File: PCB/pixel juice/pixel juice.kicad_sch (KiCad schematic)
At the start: 39 parts, among them J1 n8 Bus Connector, J2 Conn_01x03_Male, J3 PJRAN3X1U03X, U1 TMS9128, U2 TMS4416, U3 TMS4416, U4 74LS32, U5 LM1881, U6 4066, U7 AD8054, Y1 10.738635Mhz

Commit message: horizontal layout for vram but i want to try vertical
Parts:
- added J4: AUDIO_CLK, Connector_PinHeader_2.54mm:PinHeader_1x02_P2.54mm_Vertical, symbol Connector:Conn_01x02_Male
- added unit 4 of U4
- added unit 3 of U4
- C1, C12, C13, C14, C15, C2, C3, C7, C8: footprint Capacitor_THT:C_Disc_D5.0mm_W2.5mm_P2.50mm -> Capacitor_SMD:C_0805_2012Metric_Pad1.18x1.45mm_HandSolder
- J2: value Conn_01x03_Male -> IRQ_SEL
- R1, R10, R11, R12, R13, R2, R3, R4, R5, R6, R7, R8, R9: footprint Resistor_THT:R_Axial_DIN0207_L6.3mm_D2.5mm_P7.62mm_Horizontal -> Resistor_SMD:R_0805_2012Metric_Pad1.20x1.40mm_HandSolder
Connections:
- net GND: now also U4.10, U4.12, U4.13, U4.9
- net AUDIO_CLK_{OUT}: now reaches J1.6 (Pin_6)
- net AUDIO_CLK_{OUT}: now also J4.1 (Pin_1)
- net AUDIO_CLK_{IN}: now reaches U1.37 (CPUCLOCK)
- net AUDIO_CLK_{IN}: now also J4.2 (Pin_2)

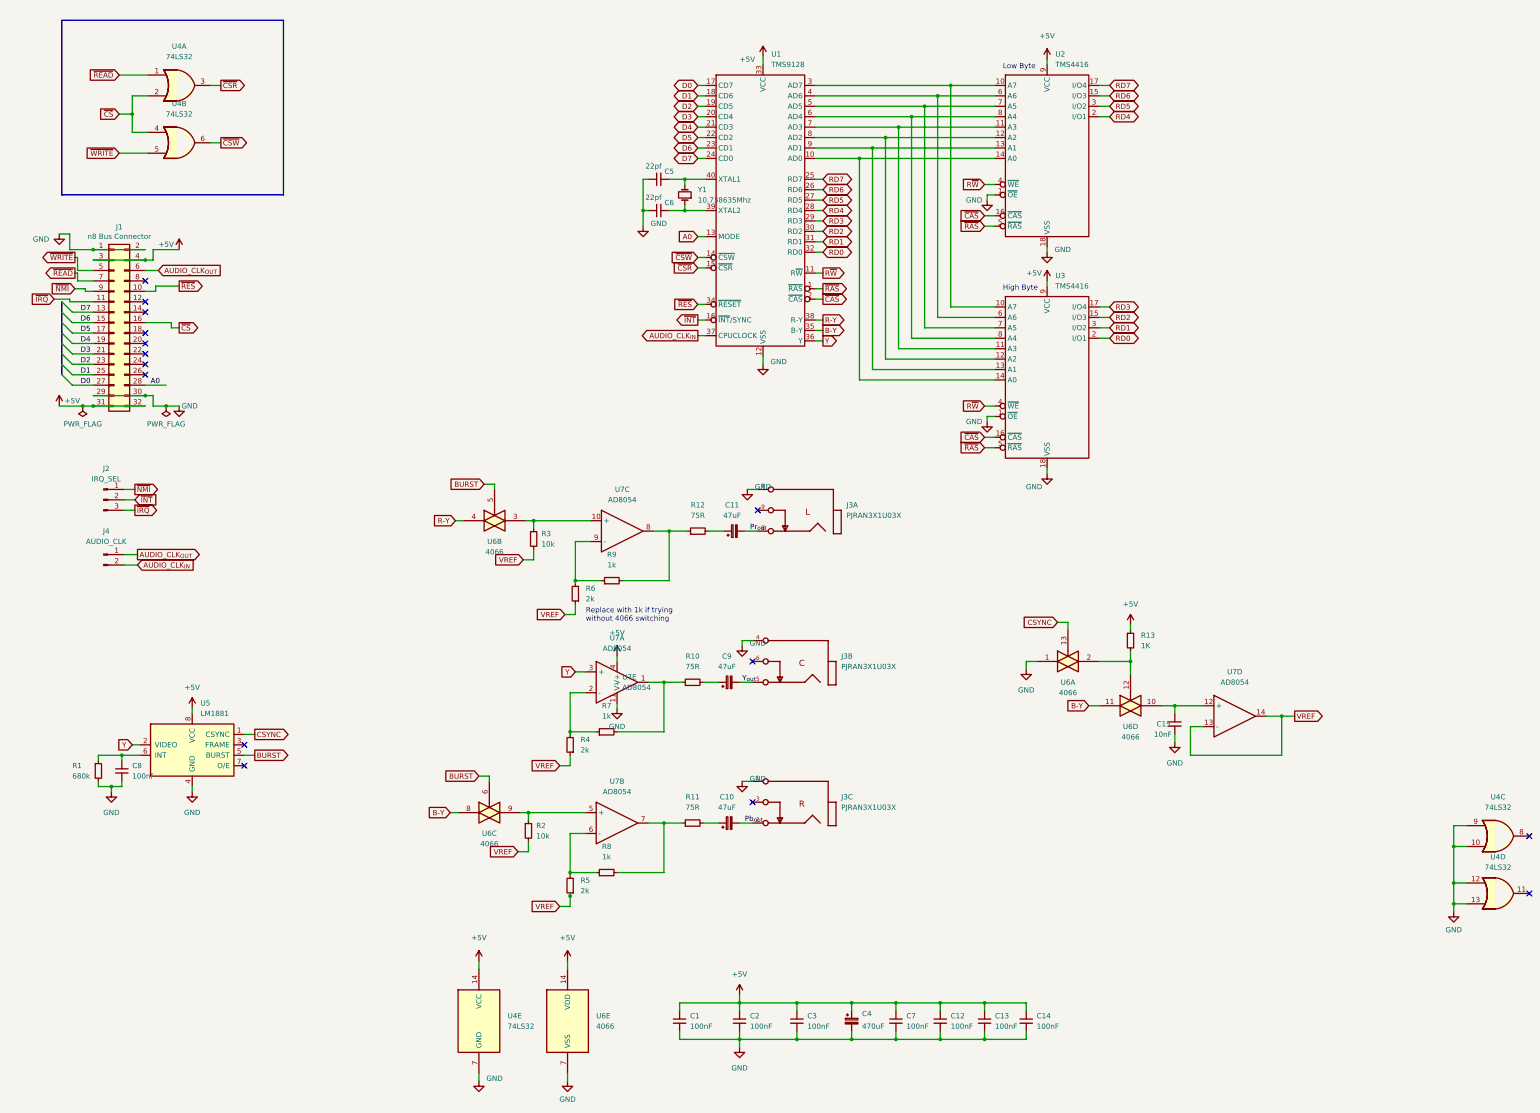
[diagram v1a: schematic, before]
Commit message: Video card + bus driver changes
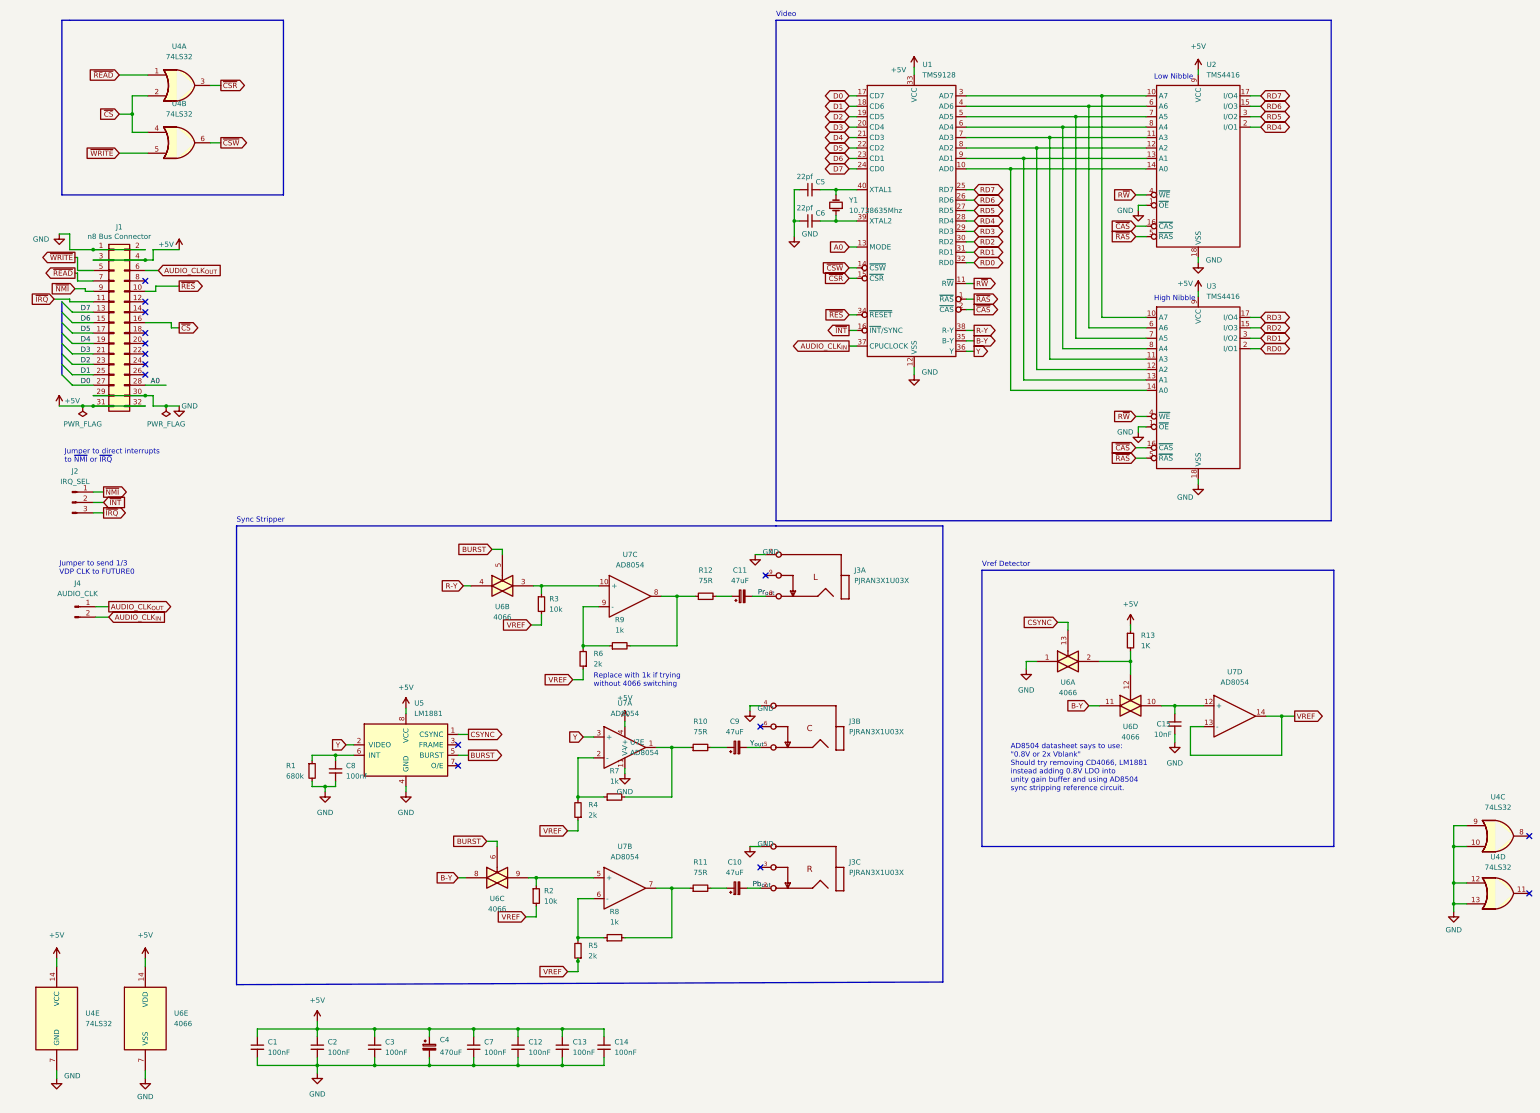
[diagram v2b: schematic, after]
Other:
- note added: "AD8504 datasheet says to use: "0.8V or 2x Vblank" Should try removing CD4066, LM1881 instead adding 0.8V LDO into unity gain buffer and using AD8504 sync stripping reference circuit."
- note added: "High Nibble"
- note added: "Jumper to direct interrupts to ~{NMI} or ~{IRQ}"
- note added: "Jumper to send 1/3 VDP CLK to FUTURE0"
- note added: "Low Nibble"
- note added: "Sync Stripper"
- note added: "Video"
- note added: "Vref Detector"
- note removed: "High Byte"
- note removed: "Low Byte"
- company: (none) -> Nate Rivard
- title: (none) -> Pixel Juice
- moved on the sheet: C1, C10, C11, C12, C13, C14, C2, C3, C4, C5, C6, C7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

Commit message: going to make v1 of the video card modular
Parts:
- added C?: 100nf, symbol Device:C_Small
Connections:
- net Y: now also C?.1; no longer U5.2 (VIDEO)
- net BURST renamed ~{BURST}
- new net: C?.2, U5.2 (VIDEO)
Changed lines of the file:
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@@
   (junction (at 135.89 266.065) (diameter 0) (color 0 0 0 0)
   )
-  (junction (at 150.495 249.555) (diameter 0) (color 0 0 0 0)
-  )
   (junction (at 363.855 230.505) (diameter 0) (color 0 0 0 0)
   )
@@
     (stroke (width 0) (type default) (color 0 0 0 0))
   )
-  (wire (pts (xy 150.495 252.095) (xy 150.495 249.555))
+  (wire (pts (xy 150.495 249.555) (xy 150.495 252.095))
     (stroke (width 0) (type default) (color 0 0 0 0))
   )
@@
     (stroke (width 0) (type default) (color 0 0 0 0))
   )
+  (wire (pts (xy 83.82 196.85) (xy 86.36 196.85))
+    (stroke (width 0) (type default) (color 0 0 0 0))
+  )
   (wire (pts (xy 38.735 52.705) (xy 45.72 52.705))
     (stroke (width 0) (type default) (color 0 0 0 0))
@@
     (stroke (width 0) (type default) (color 0 0 0 0))
   )
-  (wire (pts (xy 150.495 248.92) (xy 150.495 249.555))
-    (stroke (width 0) (type default) (color 0 0 0 0))
-  )
   (wire (pts (xy 295.91 187.325) (xy 295.91 189.23))
     (stroke (width 0) (type default) (color 0 0 0 0))
@@
     (stroke (width 0) (type default) (color 0 0 0 0))
   )
-  (wire (pts (xy 93.98 196.85) (xy 95.885 196.85))
+  (wire (pts (xy 91.44 196.85) (xy 95.885 196.85))
     (stroke (width 0) (type default) (color 0 0 0 0))
   )
@@
     )
   )
-  (global_label "BURST" (shape output) (at 123.825 199.39 0) (fields_autoplaced)
+  (global_label "~{BURST}" (shape output) (at 123.825 199.39 0) (fields_autoplaced)
     (effects (font (size 1.27 1.27)) (justify left))
     (property "Intersheet References" "${INTERSHEET_REFS}" (id 0) (at 132.1968 199.3106 0)
@@
     )
   )
-  (global_label "BURST" (shape input) (at 129.54 149.225 180) (fields_autoplaced)
+  (global_label "~{BURST}" (shape input) (at 129.54 149.225 180) (fields_autoplaced)
     (effects (font (size 1.27 1.27)) (justify right))
     (property "Intersheet References" "${INTERSHEET_REFS}" (id 0) (at 121.1682 149.1456 0)
@@
     )
   )
-  (global_label "Y" (shape input) (at 93.98 196.85 180) (fields_autoplaced)
+  (global_label "Y" (shape input) (at 83.82 196.85 180) (fields_autoplaced)
     (effects (font (size 1.27 1.27)) (justify right))
-    (property "Intersheet References" "${INTERSHEET_REFS}" (id 0) (at 90.5672 196.7706 0)
+    (property "Intersheet References" "${INTERSHEET_REFS}" (id 0) (at 80.4072 196.7706 0)
       (effects (font (size 1.27 1.27)) (justify right) hide)
     )
@@
     )
   )
-  (global_label "BURST" (shape input) (at 128.27 220.345 180) (fields_autoplaced)
+  (global_label "~{BURST}" (shape input) (at 128.27 220.345 180) (fields_autoplaced)
     (effects (font (size 1.27 1.27)) (justify right))
     (property "Intersheet References" "${INTERSHEET_REFS}" (id 0) (at 119.8982 220.2656 0)
@@
     (pin "7")
   )
+  (symbol (lib_id "Device:C_Small") (at 88.9 196.85 90) (unit 1)
+    (in_bom yes) (on_board yes) (fields_autoplaced)
+    (property "Reference" "C?" (id 0) (at 88.9063 190.5 90))
+    (property "Value" "100nf" (id 1) (at 88.9063 193.04 90))
+    (property "Footprint" "" (id 2) (at 88.9 196.85 0)
+      (effects (font (size 1.27 1.27)) hide)
+    )
+    (property "Datasheet" "~" (id 3) (at 88.9 196.85 0)
+      (effects (font (size 1.27 1.27)) hide)
+    )
+    (pin "1")
+    (pin "2")
+  )
   (symbol (lib_id "power:GND") (at 45.085 278.13 0) (unit 1)
     (in_bom yes) (on_board yes) (fields_autoplaced)
@@
       (reference "C15") (unit 1) (value "10nF") (footprint "Capacitor_SMD:C_0805_2012Metric_Pad1.18x1.45mm_HandSolder")
     )
+    (path "/08ef7103-1e41-4907-b04e-4ac6a9c1a1f7"
+      (reference "C?") (unit 1) (value "100nf") (footprint "")
+    )
     (path "/00000000-0000-0000-0000-0000604c03ac"

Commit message: Added amp stages
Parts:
- removed C10, C11, C9: 47uF, Capacitor_THT:CP_Radial_D4.0mm_P2.00mm, symbol Device:C_Polarized_Small
- removed C12, C13, C14: 100nF, Capacitor_SMD:C_0805_2012Metric_Pad1.18x1.45mm_HandSolder, symbol Device:C_Small
- removed C15: 10nF, Capacitor_SMD:C_0805_2012Metric_Pad1.18x1.45mm_HandSolder, symbol Device:C_Small
- removed C8: 100nf, Capacitor_SMD:C_0805_2012Metric_Pad1.18x1.45mm_HandSolder, symbol Device:C_Small
- removed C?: 100nf, symbol Device:C_Small
- removed J3: PJRAN3X1U03X, PJRAN3X1U03X:PJRAN3X1U01X, symbol PJRAN3X1U03X:PJRAN3X1U03X
- removed R1: 680k, Resistor_SMD:R_0805_2012Metric_Pad1.20x1.40mm_HandSolder, symbol Device:R_Small
- removed R10, R11, R12: 75R, Resistor_SMD:R_0805_2012Metric_Pad1.20x1.40mm_HandSolder, symbol Device:R_Small
- removed R13: 1K, Resistor_SMD:R_0805_2012Metric_Pad1.20x1.40mm_HandSolder, symbol Device:R_Small
- removed R2, R3: 10k, Resistor_SMD:R_0805_2012Metric_Pad1.20x1.40mm_HandSolder, symbol Device:R_Small
- removed R4, R5, R6: 2k, Resistor_SMD:R_0805_2012Metric_Pad1.20x1.40mm_HandSolder, symbol Device:R_Small
- removed R7, R8, R9: 1k, Resistor_SMD:R_0805_2012Metric_Pad1.20x1.40mm_HandSolder, symbol Device:R_Small
- removed U5: LM1881, Package_DIP:DIP-8_W7.62mm, symbol Video:LM1881
- removed U6: 4066, Package_DIP:DIP-14_W7.62mm_Socket, symbol 4xxx:4066
- removed U7: AD8054, Package_SO:SOIC-14_3.9x8.7mm_P1.27mm, symbol VDP:AD8054
- added J4: PJRAN3X1U03X, PJRAN3X1U03X:PJRAN3X1U01X, symbol PJRAN3X1U03X:PJRAN3X1U03X
- added J5: TO_AMP, Connector_PinSocket_2.54mm:PinSocket_1x05_P2.54mm_Vertical, symbol Connector:Conn_01x05_Female
- added J6: FROM_AMP, Connector_PinSocket_2.54mm:PinSocket_1x05_P2.54mm_Vertical, symbol Connector:Conn_01x05_Female
- renumbered C5 to C1, C6 to C2, C1 to C3, C2 to C4, C3 to C5, C4 to C6, J4 to J3
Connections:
- net +5V: now also J5.1 (Pin_1), J6.5 (Pin_5)
- net B-Y: now also J5.4 (Pin_4)
- net GND: now also J4.1, J4.4, J4.7, J5.5 (Pin_5), J6.1 (Pin_1)
- net R-Y: now also J5.2 (Pin_2)
- net Y: now also J5.3 (Pin_3)
- net Y_{out}: now also J4.5, J6.3 (Pin_3)
- new net B-Y_{out}: J4.2, J6.2 (Pin_2)
- new net R-Y_{out}: J4.8, J6.4 (Pin_4)
- no-connect marks 15 -> 13
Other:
- note added: "Address Decoding"
- note removed: "AD8504 datasheet says to use: "0.8V or 2x Vblank" Should try removing CD4066, LM1881 instead adding 0.8V LDO into unity gain buffer and using AD8504 sync stripping reference circuit."
- note removed: "Replace with 1k if trying without 4066 switching"
- note removed: "Sync Stripper"
- note removed: "Vref Detector"
- moved on the sheet: U4A, U4B, U4C, U4D
